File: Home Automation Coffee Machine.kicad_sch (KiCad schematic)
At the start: 39 parts, among them J1 Conn_01x08_Male

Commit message: revision 2.3
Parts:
- removed PC3: 2.2uF, Capacitor_SMD:C_1206_3216Metric, symbol Device:C
- added BZ1: Buzzer, Buzzer_Beeper:MagneticBuzzer_Kobitone_254-EMB84Q-RO, symbol Device:Buzzer
- added WaterLevel1: WaterLevel, Connector_JST:JST_EH_B2B-EH-A_1x02_P2.50mm_Vertical, symbol Connector:Conn_01x02_Female
- ESP32-S3-WROOM1: renamed from ESP32-WROOM32; value ESP32-WROOM-32 -> ESP32-S3-WROOM1
- ExtSW1: footprint TerminalBlock_4Ucon:TerminalBlock_4Ucon_1x03_P3.50mm_Horizontal -> TerminalBlock_4Ucon:TerminalBlock_4Ucon_1x03_P3.50mm_Vertical
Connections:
- net 3V3: now also WaterLevel1.1 (Pin_1)
- net GND: now also BZ1.2 (+); no longer ESP32-S3-WROOM1.24 (IO2)
- net IO19_ renamed IO19_BUZ
- net IO19_BUZ: now also BZ1.1 (-)
- new net IO24_WaterLevel: ESP32-S3-WROOM1.24 (IO2), WaterLevel1.2 (Pin_2)
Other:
- moved on the sheet: NEXTIONLCD1

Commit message: rev. 2.4
improved  relay connectivity. New 3.3V power converter.
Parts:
- removed HX4002B1: PWIC, AeonLabs:HX4002 SOT95 P280X125-6N, symbol HX4002:HX4002
- removed HX4002B2: PWIC1, AeonLabs:HX4002 SOT95 P280X125-6N, symbol HX4002:HX4002
- removed PC1, PC2, PC4: 2.2uF, Capacitor_SMD:C_1206_3216Metric, symbol Device:C
- added Coffee1: QD2, TestPoint:TestPoint_Pad_Bridge_1.0x1.0mm, symbol Connector:TestPoint_2Pole
- added Grinder1: QD3, TestPoint:TestPoint_Pad_Bridge_1.0x1.0mm, symbol Connector:TestPoint_2Pole
- added MC1, MC2: 28uF, Capacitor_SMD:C_0805_2012Metric_Pad1.18x1.45mm_HandSolder, symbol Device:C
- added MD1: SS36, Diode_SMD:D_2010_5025Metric_Pad1.52x2.65mm_HandSolder, symbol Device:D_Schottky
- added ML1: ????, Inductor_SMD:L_0805_2012Metric_Pad1.15x1.40mm_HandSolder, symbol Device:L
- added MR1: 2.2k, Resistor_SMD:R_0805_2012Metric_Pad1.20x1.40mm_HandSolder, symbol Device:R
- added MR2: 5V=15K; 3.3v=10k, Resistor_SMD:R_0805_2012Metric_Pad1.20x1.40mm_HandSolder, symbol Device:R
- added MT_VIN1: VIN, TestPoint:TestPoint_Pad_D1.5mm, symbol Connector:TestPoint
- added MT_VOUT1: VOUT, TestPoint:TestPoint_Pad_D1.5mm, symbol Connector:TestPoint
- added Q1, Q2, Q3: 2TY, Package_TO_SOT_SMD:SOT-23, symbol Transistor_FET:BSS138
- added QR1, QR2, QR3: 4K7, Resistor_SMD:R_0805_2012Metric_Pad1.20x1.40mm_HandSolder, symbol Device:R
- added U1: MT3608, Converter_DCDC:MT3608 SOT95P280X145-6N, symbol Power_Management:MT3608
- added h20: QD1, TestPoint:TestPoint_Pad_Bridge_1.0x1.0mm, symbol Connector:TestPoint_2Pole
- ExtPW1: footprint TerminalBlock_4Ucon:TerminalBlock_4Ucon_1x02_P3.50mm_Vertical -> Connector_JST:JST_PH_B2B-PH-K_1x02_P2.00mm_Vertical
- ExtSW1: footprint TerminalBlock_4Ucon:TerminalBlock_4Ucon_1x03_P3.50mm_Vertical -> Connector_JST:JST_PH_B3B-PH-K_1x03_P2.00mm_Vertical
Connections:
- net 3V3: now also MC2.1, MD1.1 (K), MR2.1, MT_VOUT1.1, Q1.2 (S), Q2.2 (S), Q3.2 (S)
- net 5V0: now also MC1.1, ML1.1, MT_VIN1.1, U1.4 (EN), U1.5 (IN)
- net GND: now also MC1.2, MC2.2, MR1.2, U1.2 (GND)
- net IO04_H2O: now also QR1.1, h20.1; no longer ExtSW1.3 (Pin_3)
- net IO12_grinder: no longer names the net of ExtSW1.1 (Pin_1)
- net IO12_grinder: now also Grinder1.2, Q2.3 (D); no longer ESP32-S3-WROOM1.14 (IO12)
- net IO15_Coffee: no longer names the net of ExtSW1.2 (Pin_2)
- net IO15_Coffee: now also Coffee1.2, Q3.3 (D); no longer ESP32-S3-WROOM1.23 (IO15)
- new net: Q2.1 (G), QR2.2
- new net: MD1.2 (A), ML1.2, U1.1 (SW)
- new net: MR1.1, MR2.2, U1.3 (FB)
- new net: ExtSW1.3 (Pin_3), Q1.3 (D), h20.2
- new net: Q1.1 (G), QR1.2
- new net: Q3.1 (G), QR3.2
- new net IO12_Coffee: Coffee1.1, ESP32-S3-WROOM1.14 (IO12), QR3.1
- new net IO15_grinder: ESP32-S3-WROOM1.23 (IO15), Grinder1.1, QR2.1
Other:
- note added: "Power Supply"
- moved on the sheet: AC220IN1, BZ1, CJ11, CJ12, CRX1, CRX2, CTX1, CTX2, DS1, ENR1, ESP32-S3-WROOM1, ESPC1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

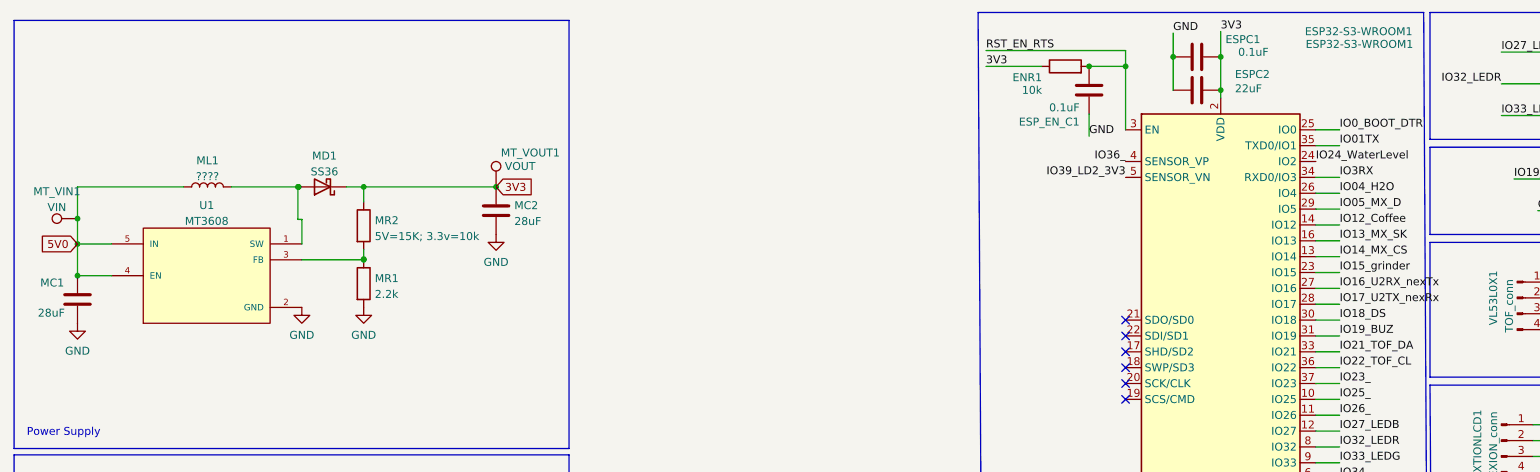
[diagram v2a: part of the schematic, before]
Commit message: rev. 2.5
correction to the power supply.
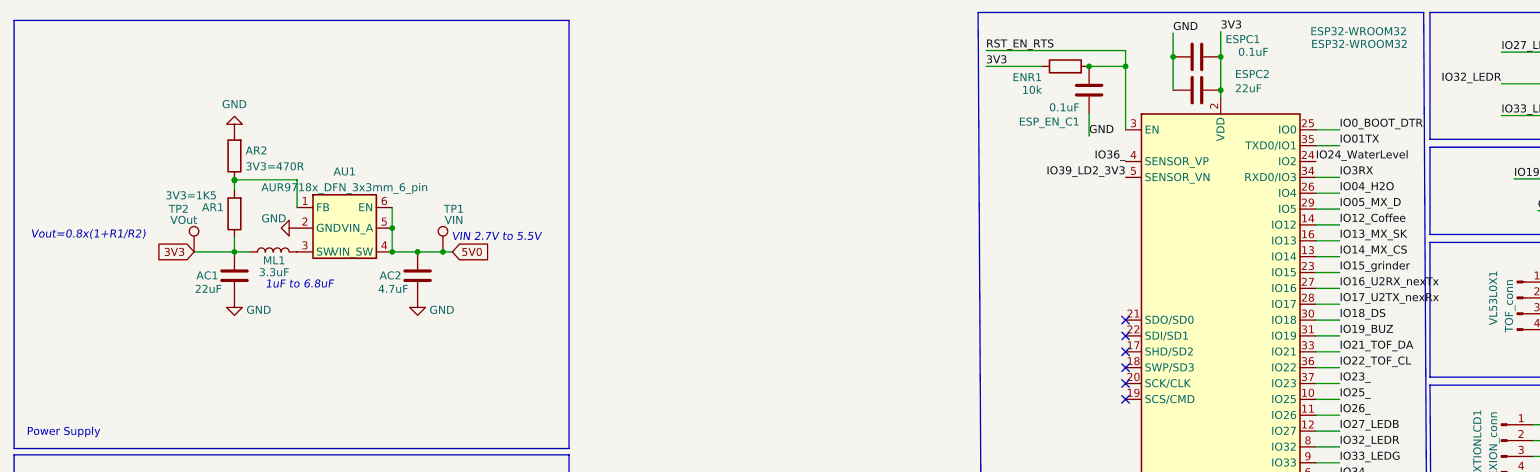
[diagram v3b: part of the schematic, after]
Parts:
- removed MC1, MC2: 28uF, Capacitor_SMD:C_0805_2012Metric_Pad1.18x1.45mm_HandSolder, symbol Device:C
- removed MD1: SS36, Diode_SMD:D_2010_5025Metric_Pad1.52x2.65mm_HandSolder, symbol Device:D_Schottky
- removed MR1: 2.2k, Resistor_SMD:R_0805_2012Metric_Pad1.20x1.40mm_HandSolder, symbol Device:R
- removed MR2: 5V=15K; 3.3v=10k, Resistor_SMD:R_0805_2012Metric_Pad1.20x1.40mm_HandSolder, symbol Device:R
- removed MT_VIN1: VIN, TestPoint:TestPoint_Pad_D1.5mm, symbol Connector:TestPoint
- removed MT_VOUT1: VOUT, TestPoint:TestPoint_Pad_D1.5mm, symbol Connector:TestPoint
- removed U1: MT3608, Converter_DCDC:MT3608 SOT95P280X145-6N, symbol Power_Management:MT3608
- added AC1: 22uF, Capacitor_SMD:C_0805_2012Metric_Pad1.18x1.45mm_HandSolder, symbol Device:C
- added AC2: 4.7uF, Capacitor_SMD:C_0805_2012Metric_Pad1.18x1.45mm_HandSolder, symbol Device:C
- added AR1: 3V3=1K5, Resistor_SMD:R_0805_2012Metric_Pad1.20x1.40mm_HandSolder, symbol Device:R
- added AR2: 3V3=470R, Resistor_SMD:R_0805_2012Metric_Pad1.20x1.40mm_HandSolder, symbol Device:R
- added AU1: AUR9718x_DFN_3x3mm_6_pin, Package_DFN_QFN:AUR9718 3x3mm 6 pin, symbol Power_Management:AUR9718x_DFN_3x3mm_6_pin
- added TP1: VIN, TestPoint:TestPoint_Pad_D1.0mm, symbol Connector:TestPoint
- added TP2: VOut, TestPoint:TestPoint_Pad_D1.0mm, symbol Connector:TestPoint
- ESP32-WROOM32: renamed from ESP32-S3-WROOM1; value ESP32-S3-WROOM1 -> ESP32-WROOM32
- ML1: value ???? -> 3.3uF; footprint Inductor_SMD:L_0805_2012Metric_Pad1.15x1.40mm_HandSolder -> Inductor_SMD:L_1210_3225Metric
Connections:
- net 3V3: now also ML1.1, AC1.1, AR1.1, TP2.1
- net 5V0: now also AC2.1, AU1.4 (VIN_SW), AU1.5 (VIN_A), AU1.6 (EN), TP1.1; no longer ML1.1
- net GND: now also AC1.2, AC2.2, AR2.2, AU1.2 (GND)
- net at ML1.2: now also AU1.3 (SW)
- new net: AR1.2, AR2.1, AU1.1 (FB)
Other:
- note added: "1uF to 6.8uF"
- note added: "VIN 2.7V to 5.5V"
- note added: "Vout=0.8x(1+R1/R2)"
